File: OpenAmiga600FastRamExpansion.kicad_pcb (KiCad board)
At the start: 2 copper layers, 72.3 x 72.5 mm, 27 parts, among them J1 MC68000_PLCC68, P1 JTAG_CONNECTOR, P98 SCREW_HOLE, P99 OSHW_LOGO, U1 74LS157, U2 74LS157, U3 HYB5118160BSJ, U4 HYB5118160BSJ, U5 ATF1502AS-10JU44

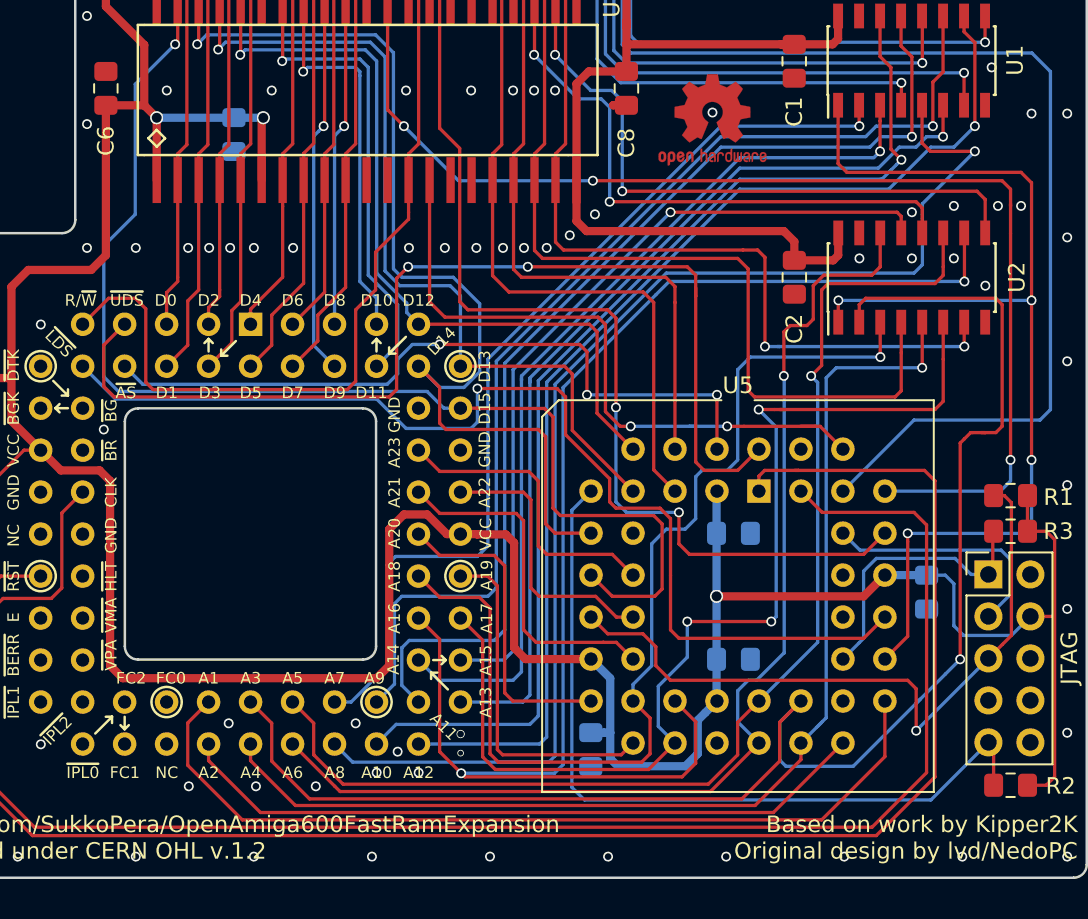
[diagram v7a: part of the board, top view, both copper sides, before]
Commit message: Ground stitching done
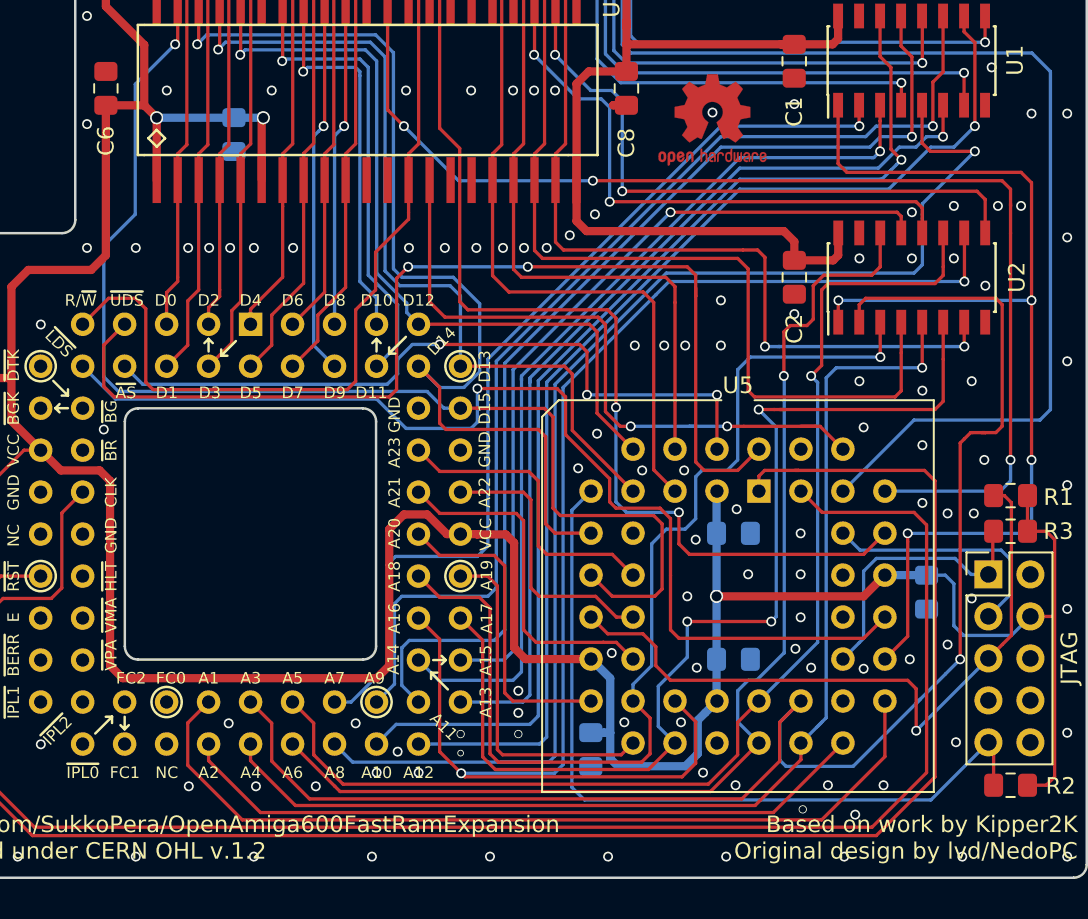
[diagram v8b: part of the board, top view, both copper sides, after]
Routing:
- net GND: vias 99 -> 146
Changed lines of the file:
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@@
     (thickness 1.6)
     (drawings 102)
-    (tracks 1152)
+    (tracks 1199)
     (zones 0)
     (modules 27)
@@
   (title_block
     (title OpenAmiga600FastRamExpansion)
-    (date 2019-02-25)
+    (date 2019-02-26)
     (rev 1git)
     (company SukkoPera)
@@
     (45 Margin user hide)
     (46 B.CrtYd user hide)
-    (47 F.CrtYd user)
+    (47 F.CrtYd user hide)
     (49 F.Fab user hide)
   )
@@
     (effects (font (size 0.7 0.7) (thickness 0.15)))
   )
-  (gr_text ~BG (at 124.2695 98.2345 90) (layer F.SilkS)
+  (gr_text ~BG (at 124.2695 98.298 90) (layer F.SilkS)
     (effects (font (size 0.7 0.7) (thickness 0.15)))
   )
@@
   (segment (start 154.648 79.765) (end 155.448 79.765) (width 0.5) (layer F.Cu) (net 18))
   (segment (start 154.639 79.756) (end 154.648 79.765) (width 0.5) (layer F.Cu) (net 18))
+  (via (at 148.9075 115.189) (size 0.6) (drill 0.4) (layers F.Cu B.Cu) (net 18))
+  (via (at 148.9075 116.5225) (size 0.6) (drill 0.4) (layers F.Cu B.Cu) (net 18))
+  (via (at 148.9075 117.8052) (size 0.5) (drill 0.4) (layers F.Cu B.Cu) (net 18))
+  (via (at 154.559 112.903) (size 0.6) (drill 0.4) (layers F.Cu B.Cu) (net 18))
+  (via (at 155.321 117.094) (size 0.6) (drill 0.4) (layers F.Cu B.Cu) (net 18))
+  (via (at 158.75 117.094) (size 0.6) (drill 0.4) (layers F.Cu B.Cu) (net 18))
+  (via (at 160.0835 120.142) (size 0.6) (drill 0.4) (layers F.Cu B.Cu) (net 18))
+  (via (at 162.052 120.904) (size 0.6) (drill 0.4) (layers F.Cu B.Cu) (net 18))
+  (via (at 166.116 122.3645) (size 0.5) (drill 0.4) (layers F.Cu B.Cu) (net 18))
+  (via (at 169.291 122.682) (size 0.6) (drill 0.4) (layers F.Cu B.Cu) (net 18))
+  (via (at 167.64 120.904) (size 0.6) (drill 0.4) (layers F.Cu B.Cu) (net 18))
+  (via (at 171.0055 120.904) (size 0.6) (drill 0.4) (layers F.Cu B.Cu) (net 18))
+  (via (at 175.387 118.3005) (size 0.6) (drill 0.4) (layers F.Cu B.Cu) (net 18))
+  (via (at 159.7025 113.792) (size 0.6) (drill 0.4) (layers F.Cu B.Cu) (net 18))
+  (via (at 165.6715 112.649) (size 0.6) (drill 0.4) (layers F.Cu B.Cu) (net 18))
+  (via (at 166.624 113.792) (size 0.6) (drill 0.4) (layers F.Cu B.Cu) (net 18))
+  (via (at 169.799 113.8555) (size 0.6) (drill 0.4) (layers F.Cu B.Cu) (net 18))
+  (via (at 172.593 113.284) (size 0.6) (drill 0.4) (layers F.Cu B.Cu) (net 18))
+  (via (at 174.879 112.395) (size 0.6) (drill 0.4) (layers F.Cu B.Cu) (net 18))
+  (via (at 165.989 110.744) (size 0.6) (drill 0.4) (layers F.Cu B.Cu) (net 18))
+  (via (at 165.989 108.1405) (size 0.6) (drill 0.4) (layers F.Cu B.Cu) (net 18))
+  (via (at 159.131 109.474) (size 0.6) (drill 0.4) (layers F.Cu B.Cu) (net 18))
+  (via (at 162.814 108.1405) (size 0.6) (drill 0.4) (layers F.Cu B.Cu) (net 18))
+  (via (at 152.527 101.727) (size 0.6) (drill 0.4) (layers F.Cu B.Cu) (net 18))
+  (via (at 153.67 99.6315) (size 0.6) (drill 0.4) (layers F.Cu B.Cu) (net 18))
+  (via (at 156.4005 101.854) (size 0.6) (drill 0.4) (layers F.Cu B.Cu) (net 18))
+  (via (at 158.9405 101.854) (size 0.6) (drill 0.4) (layers F.Cu B.Cu) (net 18))
+  (via (at 159.639 106.045) (size 0.6) (drill 0.4) (layers F.Cu B.Cu) (net 18))
+  (via (at 162.1155 104.2035) (size 0.6) (drill 0.4) (layers F.Cu B.Cu) (net 18))
+  (via (at 165.989 105.664) (size 0.6) (drill 0.4) (layers F.Cu B.Cu) (net 18))
+  (via (at 173.355 103.8225) (size 0.6) (drill 0.4) (layers F.Cu B.Cu) (net 18))
+  (via (at 174.879 104.4575) (size 0.6) (drill 0.4) (layers F.Cu B.Cu) (net 18))
+  (via (at 173.355 100.33) (size 0.6) (drill 0.4) (layers F.Cu B.Cu) (net 18))
+  (via (at 169.799 99.2505) (size 0.6) (drill 0.4) (layers F.Cu B.Cu) (net 18))
+  (via (at 177.1015 101.219) (size 0.6) (drill 0.4) (layers F.Cu B.Cu) (net 18))
+  (via (at 176.4665 104.4575) (size 0.6) (drill 0.4) (layers F.Cu B.Cu) (net 18))
+  (via (at 176.3395 109.601) (size 0.6) (drill 0.4) (layers F.Cu B.Cu) (net 18))
+  (via (at 155.956 94.2975) (size 0.6) (drill 0.4) (layers F.Cu B.Cu) (net 18))
+  (via (at 157.734 94.2975) (size 0.6) (drill 0.4) (layers F.Cu B.Cu) (net 18))
+  (via (at 159.004 94.2975) (size 0.6) (drill 0.4) (layers F.Cu B.Cu) (net 18))
+  (via (at 161.163 94.2975) (size 0.6) (drill 0.4) (layers F.Cu B.Cu) (net 18))
+  (via (at 161.163 91.567) (size 0.6) (drill 0.4) (layers F.Cu B.Cu) (net 18))
+  (via (at 165.608 92.3925) (size 0.6) (drill 0.4) (layers F.Cu B.Cu) (net 18))
+  (via (at 169.545 96.4565) (size 0.6) (drill 0.4) (layers F.Cu B.Cu) (net 18))
+  (via (at 173.355 97.028) (size 0.6) (drill 0.4) (layers F.Cu B.Cu) (net 18))
+  (via (at 176.3395 96.4565) (size 0.6) (drill 0.4) (layers F.Cu B.Cu) (net 18))
+  (via (at 165.608 79.6925) (size 0.6) (drill 0.4) (layers F.Cu B.Cu) (net 18))
   (segment (start 165.6 76.075) (end 167.925 76.075) (width 0.5) (layer F.Cu) (net 19))
   (segment (start 168.255 75.745) (end 168.255 74.36) (width 0.5) (layer F.Cu) (net 19))
@@
   (segment (start 148.617 89.689) (end 149.098 90.17) (width 0.2) (layer F.Cu) (net 53))
   (segment (start 148.617 84.29) (end 148.617 89.689) (width 0.2) (layer F.Cu) (net 53))
-  (segment (start 178.689 109.351) (end 178.689 107.248998) (width 0.2) (layer B.Cu) (net 54))
-  (segment (start 177.35 110.69) (end 178.689 109.351) (width 0.2) (layer B.Cu) (net 54))
-  (segment (start 178.120002 106.68) (end 178.689 107.248998) (width 0.2) (layer B.Cu) (net 54))
   (segment (start 169.576 106.68) (end 178.120002 106.68) (width 0.2) (layer B.Cu) (net 54))
+  (segment (start 178.120002 106.68) (end 178.689 107.248998) (width 0.2) (layer B.Cu) (net 54))
   (segment (start 169.576 106.68) (end 168.546 105.65) (width 0.2) (layer B.Cu) (net 54))
+  (segment (start 178.689 109.351) (end 178.689 107.248998) (width 0.2) (layer B.Cu) (net 54))
+  (segment (start 177.35 110.69) (end 178.689 109.351) (width 0.2) (layer B.Cu) (net 54))
   (via (at 155.702 99.187) (size 0.6) (drill 0.4) (layers F.Cu B.Cu) (net 55))
   (segment (start 167.163 99.187) (end 168.546 100.57) (width 0.2) (layer F.Cu) (net 55))
